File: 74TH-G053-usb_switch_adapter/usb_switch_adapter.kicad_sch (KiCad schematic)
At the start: 10 parts, among them J1 USB-C Plug, J2 USB2.0-C_SMT, SW1 SW_Push, U1 CH217K, U2 CH32V003J4M6

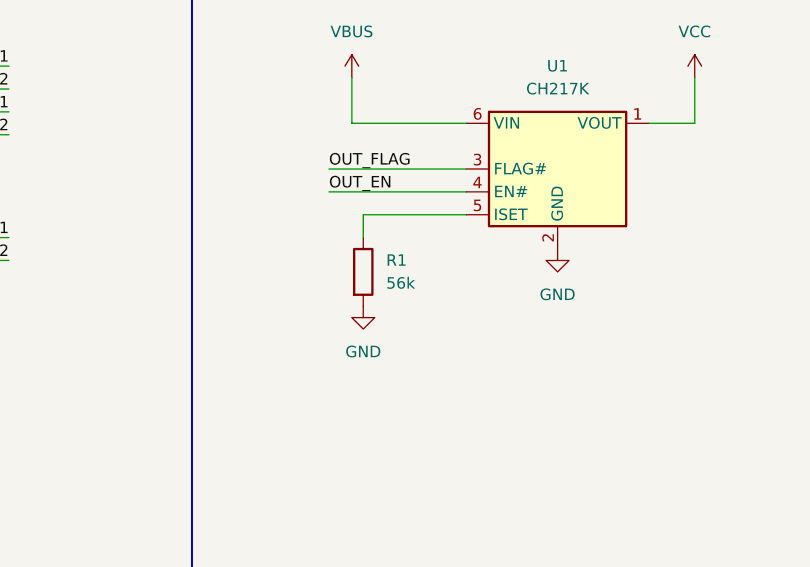
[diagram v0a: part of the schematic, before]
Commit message: USB Switch Adapter
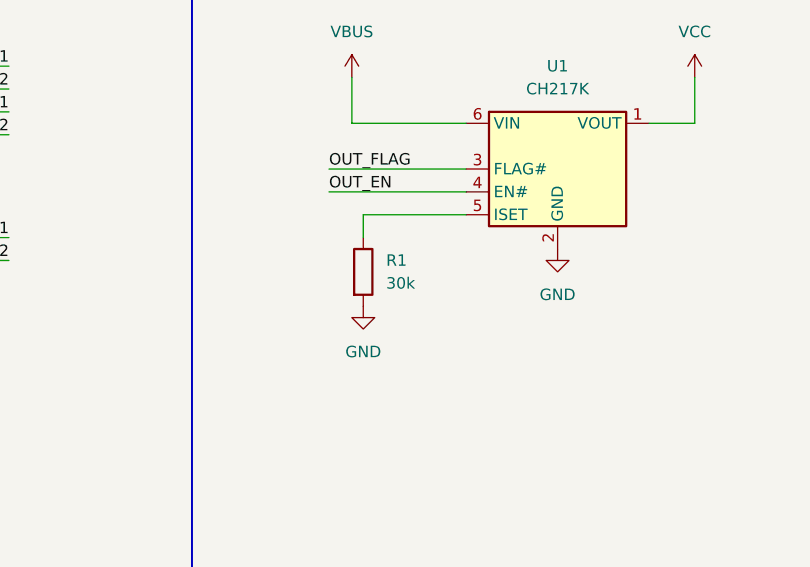
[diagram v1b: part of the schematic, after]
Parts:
- R1: value 56k -> 30k
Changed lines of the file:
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@@
 			)
 		)
-		(property "Value" "56k"
+		(property "Value" "30k"
 			(at 102.87 78.7399 0)
 			(effects

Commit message: update Document
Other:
- note added: "LED"
- note added: "MCU"
- note added: "MCU SWD-1wire"
- note added: "Switch"
- moved on the sheet: CH1
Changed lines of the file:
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@@
 	(wire
 		(pts
-			(xy 54.61 163.83) (xy 62.23 163.83)
+			(xy 44.45 163.83) (xy 52.07 163.83)
 		)
 		(stroke
@@
 	(wire
 		(pts
-			(xy 62.23 156.21) (xy 62.23 158.75)
+			(xy 52.07 156.21) (xy 52.07 158.75)
 		)
 		(stroke
@@
 	(wire
 		(pts
-			(xy 62.23 158.75) (xy 54.61 158.75)
+			(xy 52.07 158.75) (xy 44.45 158.75)
 		)
 		(stroke
@@
 	(wire
 		(pts
-			(xy 62.23 163.83) (xy 62.23 168.91)
+			(xy 52.07 163.83) (xy 52.07 168.91)
 		)
 		(stroke
@@
 	(wire
 		(pts
-			(xy 54.61 161.29) (xy 69.85 161.29)
+			(xy 44.45 161.29) (xy 59.69 161.29)
 		)
 		(stroke
@@
 		)
 	)
-	(text "Downstream"
+	(text "Switch"
 		(exclude_from_sim no)
 		(at 217.17 15.748 0)
+		(effects
+			(font
+				(size 2.54 2.54)
+			)
+			(justify left top)
+		)
+	)
+	(text "MCU SWD-1wire"
+		(exclude_from_sim no)
+		(at 14.732 128.27 0)
+		(effects
+			(font
+				(size 2.54 2.54)
+			)
+			(justify left top)
+		)
+	)
+	(text "LED"
+		(exclude_from_sim no)
+		(at 217.932 74.676 0)
+		(effects
+			(font
+				(size 2.54 2.54)
+			)
+			(justify left top)
+		)
+	)
+	(text "MCU"
+		(exclude_from_sim no)
+		(at 87.884 129.032 0)
 		(effects
 			(font
@@
 	)
 	(label "SWDIO"
-		(at 69.85 161.29 180)
+		(at 59.69 161.29 180)
 		(fields_autoplaced yes)
 		(effects
@@
 	(symbol
 		(lib_id "74th_Interface:SWD_WCH-1Wire_WITH-VCC")
-		(at 48.26 161.29 0)
+		(at 38.1 161.29 0)
 		(unit 1)
 		(exclude_from_sim no)
@@
 		(dnp no)
 		(property "Reference" "CH1"
-			(at 48.26 152.4 0)
+			(at 38.1 152.4 0)
 			(effects
 				(font
@@
 		)
 		(property "Value" "SWD 1Wire"
-			(at 48.26 154.94 0)
+			(at 38.1 154.94 0)
 			(effects
 				(font
@@
 		)
 		(property "Footprint" "74th:PinOut_Pin_3_3GND"
-			(at 45.72 156.21 0)
+			(at 35.56 156.21 0)
 			(effects
 				(font
@@
 		)
 		(property "Datasheet" ""
-			(at 45.72 156.21 0)
+			(at 35.56 156.21 0)
 			(effects
 				(font
@@
 		)
 		(property "Description" ""
-			(at 48.26 161.29 0)
+			(at 38.1 161.29 0)
 			(effects
 				(font
@@
 	(symbol
 		(lib_id "power:VBUS")
-		(at 62.23 156.21 0)
+		(at 52.07 156.21 0)
 		(unit 1)
 		(exclude_from_sim no)
@@
 		(fields_autoplaced yes)
 		(property "Reference" "#PWR04"
-			(at 62.23 160.02 0)
+			(at 52.07 160.02 0)
 			(effects
 				(font
@@
 		)
 		(property "Value" "VBUS"
-			(at 62.23 151.13 0)
+			(at 52.07 151.13 0)
 			(effects
 				(font
@@
 		)
 		(property "Footprint" ""
-			(at 62.23 156.21 0)
+			(at 52.07 156.21 0)
 			(effects
 				(font
@@
 		)
 		(property "Datasheet" ""
-			(at 62.23 156.21 0)
+			(at 52.07 156.21 0)
 			(effects
 				(font
@@
 		)
 		(property "Description" "Power symbol creates a global label with name \"VBUS\""
-			(at 62.23 156.21 0)
+			(at 52.07 156.21 0)
 			(effects
 				(font
@@
 	(symbol
 		(lib_id "power:GND")
-		(at 62.23 168.91 0)
+		(at 52.07 168.91 0)
 		(unit 1)
 		(exclude_from_sim no)
@@
 		(fields_autoplaced yes)
 		(property "Reference" "#PWR08"
-			(at 62.23 175.26 0)
+			(at 52.07 175.26 0)
 			(effects
 				(font
@@
 		)
 		(property "Value" "GND"
-			(at 62.23 173.99 0)
+			(at 52.07 173.99 0)
 			(effects
 				(font
@@
 		)
 		(property "Footprint" ""
-			(at 62.23 168.91 0)
+			(at 52.07 168.91 0)
 			(effects
 				(font
@@
 		)
 		(property "Datasheet" ""
-			(at 62.23 168.91 0)
+			(at 52.07 168.91 0)
 			(effects
 				(font
@@
 		)
 		(property "Description" "Power symbol creates a global label with name \"GND\" , ground"
-			(at 62.23 168.91 0)
-			(effects
-				(font
+			(at 52.07 168.91 0)
+			(effects
+				(font
